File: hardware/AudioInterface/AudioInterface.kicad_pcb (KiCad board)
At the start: 4 copper layers, 38 x 42 mm, 60 parts, among them J1 I2S + SPI, J2 USB_C_Receptacle_USB2.0, J3 S/PDIF, J4 CFG, SW1 RST, U1 USB3318, U2 ICE40HX8K-BG121, U3 PLL1708, U4 SP3400-02UTG, U5 GD25Q40C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

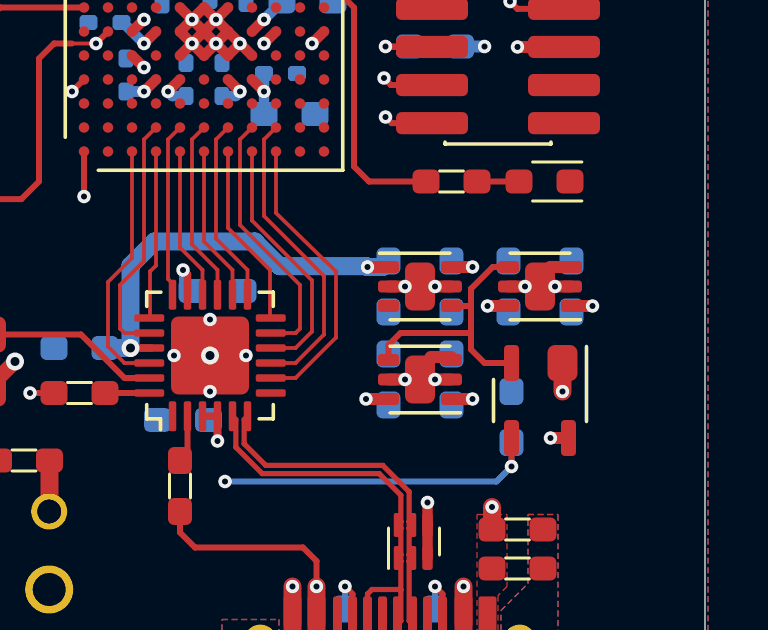
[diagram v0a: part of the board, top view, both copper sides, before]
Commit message: Improved the PSU enable/reset handling on the audio interface board
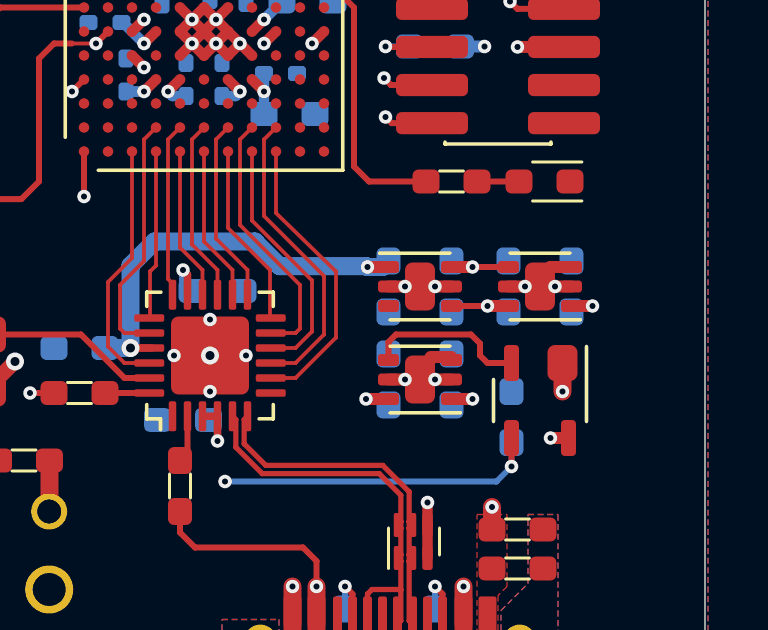
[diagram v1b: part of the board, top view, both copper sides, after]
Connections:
- U8 pad 4: /Power/~{PSU_EN} -> +3V3
- U9 pad 4: /Power/~{PSU_EN} -> +3V3
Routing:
- net /Power/~{PSU_EN}: track 9.20 -> 5.43 mm
- net +3V3: track 38.2 -> 40.6 mm
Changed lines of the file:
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@@
   (net 121 "Net-(U1-Pad23)")
   (net 122 "unconnected-(U9-Pad3)")
-  (net 123 "Net-(U7-Pad3)")
+  (net 123 "Net-(C15-Pad1)")
   (net 124 "Net-(D1-Pad2)")
-  (net 125 "Net-(U2-PadK8)")
+  (net 125 "Net-(R8-Pad1)")
   (footprint "rhais_package-qfn:WSON-6-1EP_2x2mm_P0.65mm_EP1x1.6mm" (layer "F.Cu")
     (at 194.5 121.5 180)
@@
       (net 1 "DGND") (pinfunction "GND") (pintype "power_in"))
     (pad "4" smd roundrect (at 1.05 0.65 180) (size 0.7 0.4) (layers "F.Cu" "F.Paste" "F.Mask") (roundrect_rratio 0.25)
-      (net 117 "/Power/~{PSU_EN}") (pinfunction "EN") (pintype "input"))
+      (net 4 "+3V3") (pinfunction "EN") (pintype "input"))
     (pad "5" smd roundrect (at 1.05 0 180) (size 0.7 0.4) (layers "F.Cu" "F.Paste" "F.Mask") (roundrect_rratio 0.25)
       (net 1 "DGND") (pinfunction "NC") (pintype "passive"))
@@
       (net 68 "unconnected-(U2-PadK7)") (pinfunction "IOB_89") (pintype "bidirectional+no_connect"))
     (pad "K8" smd circle locked (at 1.6 3.2 90) (size 0.35 0.35) (layers "F.Cu" "F.Paste" "F.Mask")
-      (net 125 "Net-(U2-PadK8)") (pinfunction "CDONE") (pintype "open_collector"))
+      (net 125 "Net-(R8-Pad1)") (pinfunction "CDONE") (pintype "open_collector"))
     (pad "K9" smd circle locked (at 2.4 3.2 90) (size 0.35 0.35) (layers "F.Cu" "F.Paste" "F.Mask")
       (net 112 "/Processing/COPI") (pinfunction "IOB_105_SDO") (pintype "bidirectional"))
@@
       (net 117 "/Power/~{PSU_EN}") (pinfunction "~{RST}") (pintype "output"))
     (pad "3" smd roundrect (at 1.25 0.95 180) (size 0.5 1.2) (layers "F.Cu" "F.Paste" "F.Mask") (roundrect_rratio 0.25)
-      (net 123 "Net-(U7-Pad3)") (pinfunction "~{MR}") (pintype "passive"))
+      (net 123 "Net-(C15-Pad1)") (pinfunction "~{MR}") (pintype "passive"))
     (pad "4" smd roundrect (at 1.25 -0.95 180) (size 0.5 1.2) (layers "F.Cu" "F.Paste" "F.Mask") (roundrect_rratio 0.25)
       (net 12 "+5V") (pinfunction "VCC") (pintype "power_in"))
@@
     (pad "" np_thru_hole circle locked (at 0 0 180) (size 0.75 0.75) (drill 0.75) (layers *.Cu *.Mask))
     (pad "1" smd roundrect locked (at -1.9 0 180) (size 1.2 1.8) (layers "F.Cu" "F.Paste" "F.Mask") (roundrect_rratio 0.208)
-      (net 123 "Net-(U7-Pad3)") (pinfunction "1") (pintype "passive"))
+      (net 123 "Net-(C15-Pad1)") (pinfunction "1") (pintype "passive"))
     (pad "2" smd roundrect locked (at 1.9 0 180) (size 1.2 1.8) (layers "F.Cu" "F.Paste" "F.Mask") (roundrect_rratio 0.208)
       (net 1 "DGND") (pinfunction "2") (pintype "passive"))
@@
     (descr "Mounting Hole 3.2mm, M3")
     (tags "mounting hole 3.2mm m3")
-    (property "Sheetfile" "Processor.kicad_sch")
+    (property "Sheetfile" "AudioInterface.kicad_sch")
     (property "Sheetname" "")
     (attr exclude_from_pos_files)
@@
       ) (layer "F.Fab") (width 0) (fill solid))
     (pad "1" smd roundrect (at -0.85 0) (size 0.9 0.8) (layers "F.Cu" "F.Paste" "F.Mask") (roundrect_rratio 0.25)
-      (net 125 "Net-(U2-PadK8)") (pintype "passive"))
+      (net 125 "Net-(R8-Pad1)") (pintype "passive"))
     (pad "2" smd roundrect (at 0.85 0) (size 0.9 0.8) (layers "F.Cu" "F.Paste" "F.Mask") (roundrect_rratio 0.25)
       (net 124 "Net-(D1-Pad2)") (pintype "passive"))
@@
     (descr "TE FPC connector, 12 top-side contacts, 0.5mm pitch, SMT, https://www.te.com/commerce/DocumentDelivery/DDEController?Action=showdoc&DocId=Customer+Drawing%7F1734839%7FC%7Fpdf%7FEnglish%7FENG_CD_1734839_C_C_1734839.pdf%7F4-1734839-0")
     (tags "te fpc 1734839")
-    (property "Sheetfile" "Processor.kicad_sch")
+    (property "Sheetfile" "AudioInterface.kicad_sch")
     (property "Sheetname" "")
     (solder_mask_margin 0.05)
@@
     (descr "Mounting Hole 3.2mm, M3")
     (tags "mounting hole 3.2mm m3")
-    (property "Sheetfile" "Processor.kicad_sch")
+    (property "Sheetfile" "AudioInterface.kicad_sch")
     (property "Sheetname" "")
     (attr exclude_from_pos_files)
@@
     (property "OC_DIGIKEY" "445-5667-1-ND")
     (property "OC_FARNELL" "2310559")
-    (property "Sheetfile" "Processor.kicad_sch")
+    (property "Sheetfile" "AudioInterface.kicad_sch")
     (property "Sheetname" "")
     (property "URL_DIGIKEY" "https://www.digikey.com/en/products/detail/tdk-corporation/CGA3E2X7R1E104K080AA/2443145")
@@
     (property "OC_DIGIKEY" "445-5667-1-ND")
     (property "OC_FARNELL" "2310559")
-    (property "Sheetfile" "Processor.kicad_sch")
+    (property "Sheetfile" "AudioInterface.kicad_sch")
     (property "Sheetname" "")
     (property "URL_DIGIKEY" "https://www.digikey.com/en/products/detail/tdk-corporation/CGA3E2X7R1E104K080AA/2443145")
@@
       (net 122 "unconnected-(U9-Pad3)") (pinfunction "PG") (pintype "open_collector+no_connect"))
     (pad "4" smd roundrect (at 1.05 0.65) (size 0.7 0.4) (layers "F.Cu" "F.Paste" "F.Mask") (roundrect_rratio 0.25)
-      (net 117 "/Power/~{PSU_EN}") (pinfunction "EN") (pintype "input"))
+      (net 4 "+3V3") (pinfunction "EN") (pintype "input"))
     (pad "5" smd roundrect (at 1.05 0) (size 0.7 0.4) (layers "F.Cu" "F.Paste" "F.Mask") (roundrect_rratio 0.25)
       (net 1 "DGND") (pinfunction "GND") (pintype "power_in"))
@@
     (property "MPN" "FCR684208R")
     (property "OC_DIGIKEY" "3185-FCR684208R-ND")
-    (property "Sheetfile" "Processor.kicad_sch")
+    (property "Sheetfile" "AudioInterface.kicad_sch")
     (property "Sheetname" "")
     (property "URL_DIGIKEY" "https://www.digikey.com/en/products/detail/cliff-electronic-components-ltd/FCR684208R/15283092")
@@
       ) (layer "B.Fab") (width 0) (fill solid))
     (pad "1" smd roundrect (at -0.85 0 90) (size 0.9 0.8) (layers "B.Cu" "B.Paste" "B.Mask") (roundrect_rratio 0.25)
-      (net 123 "Net-(U7-Pad3)") (pintype "passive"))
+      (net 123 "Net-(C15-Pad1)") (pintype "passive"))
     (pad "2" smd roundrect (at 0.85 0 90) (size 0.9 0.8) (layers "B.Cu" "B.Paste" "B.Mask") (roundrect_rratio 0.25)
       (net 1 "DGND") (pintype "passive"))
@@
   (segment (start 173.6 119.75) (end 173.7 119.85) (width 0.4) (layer "F.Cu") (net 4))
   (segment (start 183.25 125.825) (end 183.75 125.825) (width 0.25) (layer "F.Cu") (net 4))
+  (segment (start 193.45 120.85) (end 192.25 120.85) (width 0.2) (layer "F.Cu") (net 4))
   (segment (start 183.75 125.825) (end 183.75 126.65) (width 0.25) (layer "F.Cu") (net 4))
+  (segment (start 191.55 122.15) (end 192.75 122.15) (width 0.2) (layer "F.Cu") (net 4))
   (segment (start 169.2 115.4125) (end 170.2375 115.4125) (width 0.4) (layer "F.Cu") (net 4))
   (segment (start 173.95 123.1) (end 173 123.1) (width 0.5) (layer "F.Cu") (net 4))
@@
   (segment (start 189.4 112.4) (end 189.85 112.85) (width 0.2) (layer "In2.Cu") (net 116))
   (segment (start 189.55 109.95) (end 188.8 109.95) (width 0.2) (layer "B.Cu") (net 116))
-  (segment (start 192.2 121.575) (end 192.2 122.1) (width 0.2) (layer "F.Cu") (net 117))
-  (segment (start 192.2 122.1) (end 192.2 123.05) (width 0.2) (layer "F.Cu") (net 117))
-  (segment (start 192.15 122.15) (end 192.2 122.1) (width 0.2) (layer "F.Cu") (net 117))
-  (segment (start 192.2 123.6) (end 192.65 124.05) (width 0.2) (layer "F.Cu") (net 117))
-  (segment (start 189.85 123.05) (end 192.2 123.05) (width 0.2) (layer "F.Cu") (net 117))
-  (segment (start 193.45 120.85) (end 192.925 120.85) (width 0.2) (layer "F.Cu") (net 117))
-  (segment (start 189.45 123.95) (end 189.45 123.45) (width 0.2) (layer "F.Cu") (net 117))
-  (segment (start 192.925 120.85) (end 192.2 121.575) (width 0.2) (layer "F.Cu") (net 117))
-  (segment (start 192.65 124.05) (end 193.55 124.05) (width 0.2) (layer "F.Cu") (net 117))
-  (segment (start 189.45 123.45) (end 189.85 123.05) (width 0.2) (layer "F.Cu") (net 117))
-  (segment (start 191.55 122.15) (end 192.15 122.15) (width 0.2) (layer "F.Cu") (net 117))
-  (segment (start 192.2 123.05) (end 192.2 123.6) (width 0.2) (layer "F.Cu") (net 117))
+  (segment (start 189.45 123.35) (end 189.7 123.1) (width 0.2) (layer "F.Cu") (net 117))
+  (segment (start 192.75 124.05) (end 193.55 124.05) (width 0.2) (layer "F.Cu") (net 117))
+  (segment (start 189.7 123.1) (end 192.2 123.1) (width 0.2) (layer "F.Cu") (net 117))
+  (segment (start 192.5 123.8) (end 192.75 124.05) (width 0.2) (layer "F.Cu") (net 117))
+  (segment (start 189.45 123.95) (end 189.45 123.35) (width 0.2) (layer "F.Cu") (net 117))
+  (segment (start 192.5 123.4) (end 192.5 123.8) (width 0.2) (layer "F.Cu") (net 117))
+  (segment (start 192.2 123.1) (end 192.5 123.4) (width 0.2) (layer "F.Cu") (net 117))
   (segment (start 182.75 127.05) (end 182.5 127.3) (width 0.2) (layer "F.Cu") (net 119))
   (segment (start 182.75 125.825) (end 182.75 127.05) (width 0.2) (layer "F.Cu") (net 119))

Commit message: Completed a pile more work on the various boards that comprise the project
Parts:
- C7: value 30pF -> 30p
- J4: moved to B.Cu
- R6: moved to F.Cu
- moved D1 5.21 mm to (189.6, 117.0), turned to 90 degrees
- moved R8 4.61 mm to (189.6, 113.8), turned to -90 degrees
- moved R6 4.40 mm to (195.4, 113.5)
- turned J4 to 180 degrees
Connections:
- U2 pad A4: /Clock Generation/CSEL -> unconnected-(U2-PadA4)
- U3 pad 12: /Clock Generation/CSEL -> +3V3
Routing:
- net /Clock Generation/CSEL: track 15.1 -> 0.00 mm, vias 2 -> 0
- net Net-(R8-Pad1): track 10.0 -> 4.09 mm
- net /Processing/COPI: track 10.9 -> 6.23 mm, vias 2 -> 1
- net /Processing/CFG_CLK: track 10.7 -> 14.7 mm
- net /Processing/~{CFG_CS}: track 16.6 -> 20.6 mm
- net /Processing/~{CFG_RST}: track 6.49 -> 10.4 mm
- net /Processing/CIPO: track 12.5 -> 14.2 mm
- net +3V3: track 40.6 -> 42.2 mm
